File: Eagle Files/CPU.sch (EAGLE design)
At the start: 69 parts, among them IC1 74HC574N, IC10 74HC574N, IC11 74LS541N, IC12 CY62256LL-PC, IC13 74AS04N, IC14 74AS04N, IC15 74S283N, IC16 74S283N, IC19 74ALS04N, IC2 74LS541N, IC20 74LS541N, IC21 74LS08N, IC22 NE555, IC3 4514N, IC4 74LS04N, IC5 74HC574N, IC6 74LS541N, IC7 CY62256LL-PC, IC8 74S283N, IC9 74S283N

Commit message: Removed bugs
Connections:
- new net N$79: LED2.A, R2.2
- new net N$92: LED3.A, R3.2
- new net N$93: LED4.A, R4.2
- new net N$94: LED5.A, R5.2
- new net N$95: LED6.A, R6.2
- new net N$96: LED7.A, R7.2
- new net N$97: LED8.A, R8.2
- net BUS0: now also R1.1; no longer LED1.A, R1.2
- net BUS1: now also R2.1; no longer LED2.A, R2.2
- net BUS2: now also R3.1; no longer LED3.A, R3.2
- net BUS3: now also R4.1; no longer LED4.A, R4.2
- net BUS4: no longer LED5.A
- net BUS5: no longer LED6.A
- net BUS6: no longer LED7.A
- net BUS7: no longer LED8.A
- net GND: no longer R1.1, R2.1, R3.1, R4.1, R5.2, R6.2, R7.2, R8.2
- net N$17: now also IC13C.I
- net N$22: now also LED1.A, R1.2; no longer IC13C.I
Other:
- moved on the sheet: R1, R2, R3, R4, R5, R6, R7, R8

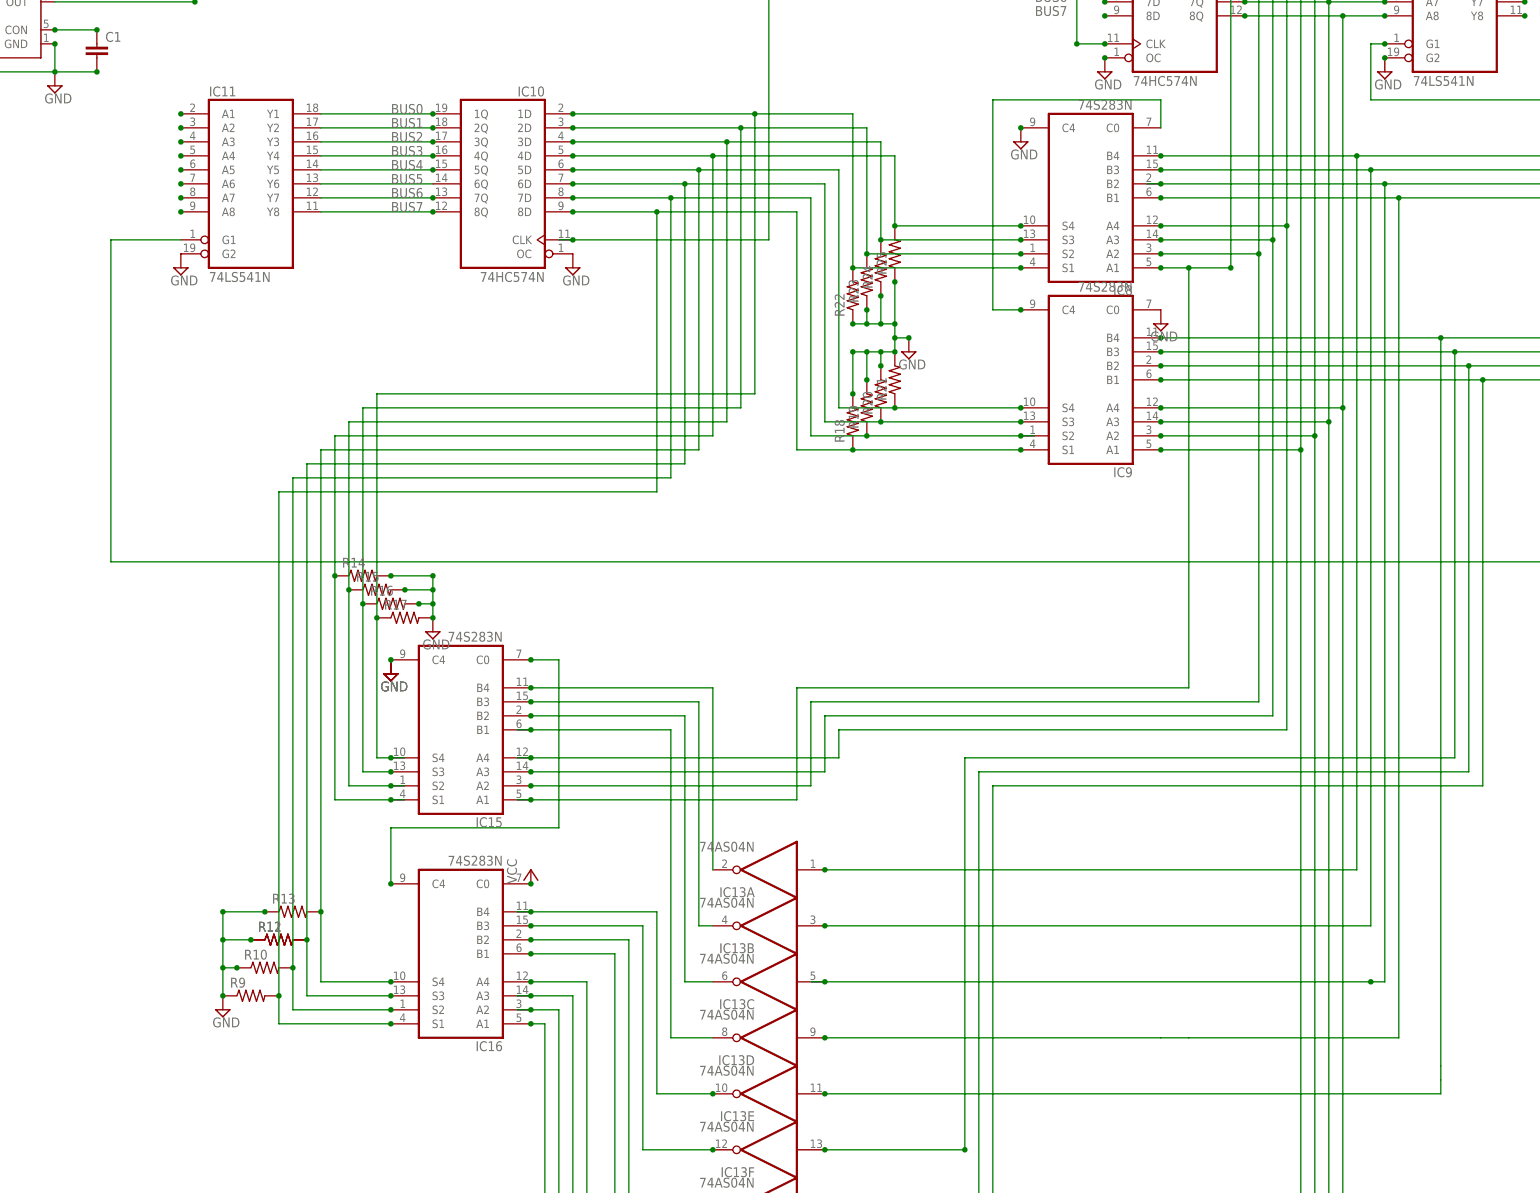
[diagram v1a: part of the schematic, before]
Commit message: Removed some bugs
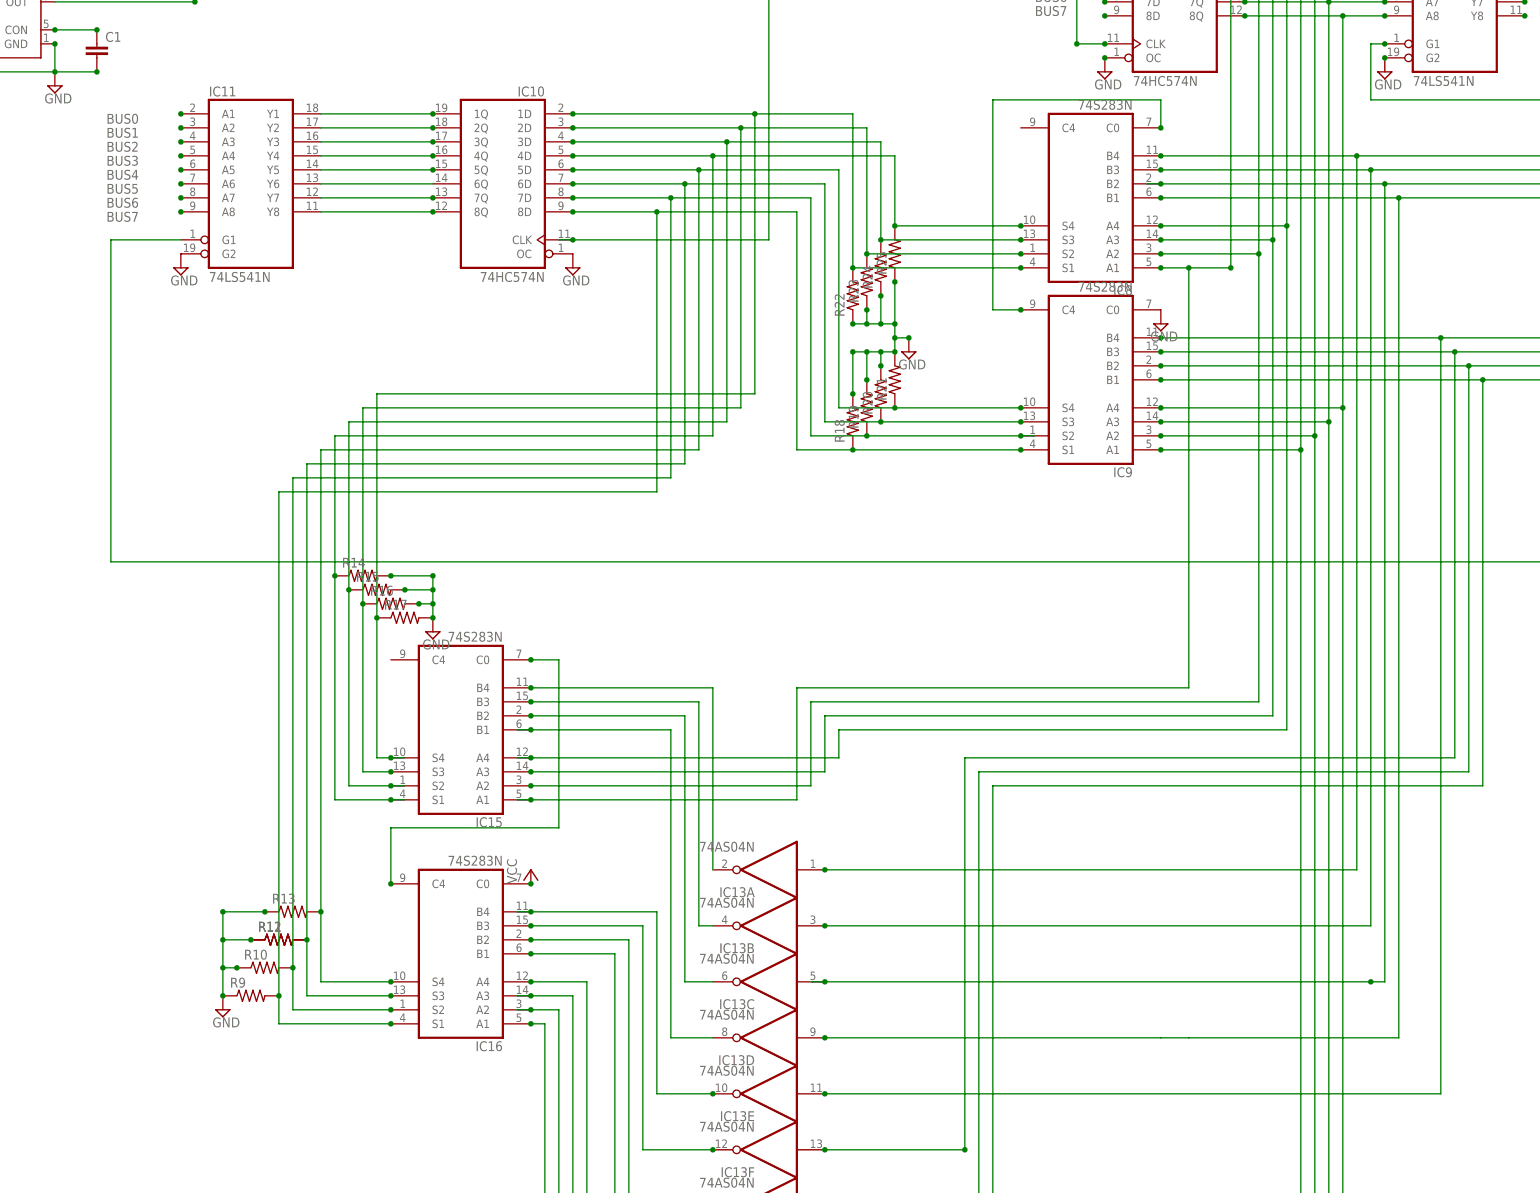
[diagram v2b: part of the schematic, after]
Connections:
- net GND: no longer IC15A.C4, IC8A.C4
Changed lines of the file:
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@@
 <part name="IC8" library="74xx-us" deviceset="74*283" device="N" technology="S"/>
 <part name="IC9" library="74xx-us" deviceset="74*283" device="N" technology="S"/>
-<part name="SUPPLY6" library="supply2" deviceset="GND" device=""/>
 <part name="IC10" library="74xx-us" deviceset="74*574" device="N" technology="HC"/>
 <part name="IC11" library="74xx-us" deviceset="74*541" device="N" technology="LS"/>
@@
 <part name="IC15" library="74xx-us" deviceset="74*283" device="N" technology="S"/>
 <part name="IC16" library="74xx-us" deviceset="74*283" device="N" technology="S"/>
-<part name="SUPPLY10" library="supply2" deviceset="GND" device=""/>
-<part name="SUPPLY11" library="supply2" deviceset="GND" device=""/>
 <part name="IC18" library="ic-package" deviceset="DIL16" device=""/>
 <part name="IC17" library="ic-package" deviceset="DIL16" device=""/>
@@
 <instance part="IC8" gate="A" x="66.04" y="27.94" rot="R180"/>
 <instance part="IC9" gate="A" x="66.04" y="-5.08" rot="R180"/>
-<instance part="SUPPLY6" gate="GND" x="53.34" y="38.1"/>
 <instance part="IC10" gate="A" x="-40.64" y="30.48" rot="MR0"/>
 <instance part="IC11" gate="A" x="-86.36" y="30.48"/>
@@
 <instance part="IC15" gate="A" x="-48.26" y="-68.58" rot="R180"/>
 <instance part="IC16" gate="A" x="-48.26" y="-109.22" rot="R180"/>
-<instance part="SUPPLY10" gate="GND" x="-60.96" y="-58.42"/>
-<instance part="SUPPLY11" gate="GND" x="-60.96" y="-58.42"/>
 <instance part="IC18" gate="G$1" x="-55.88" y="116.84" rot="R90"/>
 <instance part="IC17" gate="G$1" x="-91.44" y="116.84" rot="R90"/>
@@
 </segment>
 <segment>
-<pinref part="IC8" gate="A" pin="C4"/>
-<pinref part="SUPPLY6" gate="GND" pin="GND"/>
-<junction x="53.34" y="40.64"/>
-</segment>
-<segment>
 <pinref part="IC10" gate="A" pin="OC"/>
 <pinref part="SUPPLY8" gate="GND" pin="GND"/>
@@
 <pinref part="IC11" gate="A" pin="G2"/>
 <pinref part="SUPPLY9" gate="GND" pin="GND"/>
-</segment>
-<segment>
-<pinref part="IC15" gate="A" pin="C4"/>
-<pinref part="SUPPLY10" gate="GND" pin="GND"/>
-<pinref part="SUPPLY11" gate="GND" pin="GND"/>
-<junction x="-60.96" y="-55.88"/>
 </segment>
 <segment>
@@
 <wire x1="205.74" y1="2.54" x2="205.74" y2="66.04" width="0.1524" layer="91"/>
 <junction x="205.74" y="66.04"/>
-<wire x1="129.54" y1="-132.08" x2="129.54" y2="-129.54" width="0.1524" layer="91"/>
 <pinref part="IC13" gate="E" pin="I"/>
 <junction x="17.78" y="-134.62"/>
-<wire x1="129.54" y1="-129.54" x2="129.54" y2="2.54" width="0.1524" layer="91"/>
+<wire x1="129.54" y1="-134.62" x2="129.54" y2="2.54" width="0.1524" layer="91"/>
 <wire x1="129.54" y1="-134.62" x2="17.78" y2="-134.62" width="0.1524" layer="91"/>
-<wire x1="129.54" y1="-132.08" x2="129.54" y2="-134.62" width="0.1524" layer="91"/>
 <junction x="129.54" y="2.54"/>
 <junction x="78.74" y="2.54"/>
@@
 <pinref part="IC11" gate="A" pin="A2"/>
 <junction x="-99.06" y="40.64"/>
-<label x="-60.96" y="40.64" size="1.778" layer="95"/>
+<label x="-106.68" y="40.64" size="1.778" layer="95" rot="R180"/>
 </segment>
 <segment>
@@
 <pinref part="IC11" gate="A" pin="A3"/>
 <junction x="-99.06" y="38.1"/>
-<label x="-60.96" y="38.1" size="1.778" layer="95"/>
+<label x="-106.68" y="38.1" size="1.778" layer="95" rot="R180"/>
 </segment>
 <segment>
@@
 <pinref part="IC11" gate="A" pin="A4"/>
 <junction x="-99.06" y="35.56"/>
-<label x="-60.96" y="35.56" size="1.778" layer="95"/>
+<label x="-106.68" y="35.56" size="1.778" layer="95" rot="R180"/>
 </segment>
 <segment>
@@
 <pinref part="IC11" gate="A" pin="A5"/>
 <junction x="-99.06" y="33.02"/>
-<label x="-60.96" y="33.02" size="1.778" layer="95"/>
+<label x="-106.68" y="33.02" size="1.778" layer="95" rot="R180"/>
 </segment>
 <segment>
@@
 <pinref part="IC11" gate="A" pin="A6"/>
 <junction x="-99.06" y="30.48"/>
-<label x="-60.96" y="30.48" size="1.778" layer="95"/>
+<label x="-106.68" y="30.48" size="1.778" layer="95" rot="R180"/>
 </segment>
 <segment>
@@
 <pinref part="IC11" gate="A" pin="A7"/>
 <junction x="-99.06" y="27.94"/>
-<label x="-60.96" y="27.94" size="1.778" layer="95"/>
+<label x="-106.68" y="27.94" size="1.778" layer="95" rot="R180"/>
 </segment>
 <segment>
@@
 <pinref part="IC11" gate="A" pin="A8"/>
 <junction x="-99.06" y="25.4"/>
-<label x="-60.96" y="25.4" size="1.778" layer="95"/>
+<label x="-106.68" y="25.4" size="1.778" layer="95" rot="R180"/>
 </segment>
 <segment>
@@
 <pinref part="IC11" gate="A" pin="A1"/>
 <junction x="-99.06" y="43.18"/>
-<label x="-60.96" y="43.18" size="1.778" layer="95"/>
+<label x="-106.68" y="43.18" size="1.778" layer="95" rot="R180"/>
 </segment>
 <segment>
@@
 <wire x1="30.48" y1="-10.16" x2="20.32" y2="-10.16" width="0.1524" layer="91"/>
 <wire x1="20.32" y1="-10.16" x2="20.32" y2="33.02" width="0.1524" layer="91"/>
-<wire x1="20.32" y1="33.02" x2="0" y2="33.02" width="0.1524" layer="91"/>
+<wire x1="20.32" y1="33.02" x2="-5.08" y2="33.02" width="0.1524" layer="91"/>
 <pinref part="IC10" gate="A" pin="5D"/>
 <junction x="-27.94" y="33.02"/>
 <wire x1="-27.94" y1="33.02" x2="-5.08" y2="33.02" width="0.1524" layer="91"/>
 <pinref part="IC16" gate="A" pin="S4"/>
-<wire x1="-5.08" y1="33.02" x2="0" y2="33.02" width="0.1524" layer="91"/>
 <wire x1="-60.96" y1="-114.3" x2="-73.66" y2="-114.3" width="0.1524" layer="91"/>
 <wire x1="-73.66" y1="-114.3" x2="-73.66" y2="-101.6" width="0.1524" layer="91"/>
@@
 <wire x1="25.4" y1="-15.24" x2="15.24" y2="-15.24" width="0.1524" layer="91"/>
 <wire x1="15.24" y1="-15.24" x2="15.24" y2="27.94" width="0.1524" layer="91"/>
-<wire x1="15.24" y1="27.94" x2="0" y2="27.94" width="0.1524" layer="91"/>
+<wire x1="15.24" y1="27.94" x2="-10.16" y2="27.94" width="0.1524" layer="91"/>
 <pinref part="IC10" gate="A" pin="7D"/>
 <junction x="-27.94" y="27.94"/>
 <wire x1="-27.94" y1="27.94" x2="-10.16" y2="27.94" width="0.1524" layer="91"/>
 <pinref part="IC16" gate="A" pin="S2"/>
-<wire x1="-10.16" y1="27.94" x2="0" y2="27.94" width="0.1524" layer="91"/>
 <wire x1="-60.96" y1="-119.38" x2="-78.74" y2="-119.38" width="0.1524" layer="91"/>
 <wire x1="-78.74" y1="-119.38" x2="-78.74" y2="-111.76" width="0.1524" layer="91"/>
@@
 <wire x1="78.74" y1="45.72" x2="78.74" y2="40.64" width="0.1524" layer="91"/>
 <junction x="53.34" y="7.62"/>
-</segment>
-</net>
+<junction x="78.74" y="40.64"/>
+</segment>
+</net>

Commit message: Removed some bugs
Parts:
- removed IC17, IC18: (no value), ic-package:DIL16
- removed IC19: 74ALS04N, 74xx-us:74ALS04N
- removed IC20: 74LS541N, 74xx-us:74LS541N
- removed IC21: 74LS08N, 74xx-us:74LS08N
- removed IC22: NE555, st-microelectronics:NE555
- removed R31, R32, R33, R34, R35, R36, R37: (no value), resistor:R-US_0204/2V
- added D1, D10, D11, D12, D13, D14, D15, D16, D2, D3, D4, D5, D6, D7, D8, D9: 1N4148DO35-7, diode:1N4148DO35-7
- C1, C2: device rcl:C-EU025-024X044 -> capacitor-wima:C2,5-3
- IC1: value 74HC574N -> 74AS574N; device 74xx-us:74HC574N -> 74xx-us:74AS574N
- IC10: value 74HC574N -> 74AC283N; device 74xx-us:74HC574N -> 74xx-eu:74AC283N
- IC11, IC2: value 74LS541N -> 74AS574N; device 74xx-us:74LS541N -> 74xx-us:74AS574N
- IC12: value CY62256LL-PC -> 74LS541N; device memory-sram:CY62256LL-PC -> 74xx-us:74LS541N
- IC13: value 74AS04N -> 74HC393N; device 74xx-us:74AS04N -> 74xx-eu:74HC393N
- IC14: value 74AS04N -> 74LS541N; device 74xx-us:74AS04N -> 74xx-us:74LS541N
- IC15: value 74S283N -> 74LS32N; device 74xx-us:74S283N -> 74xx-us:74LS32N
- IC16: value 74S283N -> NE555; device 74xx-us:74S283N -> st-microelectronics:NE555
- IC3: value 4514N -> 74LS541N; device 45xx:4514N -> 74xx-us:74LS541N
- IC4: value 74LS04N -> 74LS541N; device 74xx-us:74LS04N -> 74xx-us:74LS541N
- IC5: value 74HC574N -> CY62256LL-PC; device 74xx-us:74HC574N -> memory-sram:CY62256LL-PC
- IC6: value 74LS541N -> CY62256LL-PC; device 74xx-us:74LS541N -> memory-sram:CY62256LL-PC
- IC7: value CY62256LL-PC -> 4514N; device memory-sram:CY62256LL-PC -> 45xx:4514N
- IC8: value 74S283N -> 74HC04N; device 74xx-us:74S283N -> 74xx-eu:74HC04N
- IC9: value 74S283N -> 74AC283N; device 74xx-us:74S283N -> 74xx-eu:74AC283N
- LED1, LED2, LED3, LED4, LED5, LED6, LED7, LED8: device eagle-ltspice:LED_ELD260 -> led:LED3MM
- R1, R10, R11, R12, R13, R14, R15, R16, R17, R2, R26, R27, R28, R29, R3, R30, R4, R5, R6, R7, R8, R9: device resistor:R-US_0204/2V -> rcl:R-US_MELF0102AX
- R18, R19, R20, R21, R22, R23, R24, R25: device rcl:R-US_0204/2V -> rcl:R-US_MELF0102AX
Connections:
- removed net BUS0: IC11A.A1, IC17.P0, IC1A.1D, IC20A.Y1, IC2A.Y1, IC5A.1D, IC6A.Y1, R1.1
- removed net BUS1: IC11A.A2, IC17.P1, IC1A.2D, IC20A.Y2, IC2A.Y2, IC3A.S2, IC5A.2D, IC5A.CLK, IC6A.Y2, R2.1
- removed net BUS2: IC11A.A3, IC17.P2, IC1A.3D, IC20A.Y3, IC2A.Y3, IC5A.3D, IC6A.Y3, R3.1
- removed net BUS3: IC11A.A4, IC17.P3, IC1A.4D, IC1A.CLK, IC20A.Y4, IC2A.Y4, IC3A.S0, IC5A.4D, IC6A.Y4, R4.1
- removed net BUS4: IC11A.A5, IC18.P0, IC1A.5D, IC20A.Y5, IC2A.Y5, IC5A.5D, IC6A.Y5, R5.1
- removed net BUS5: IC11A.A6, IC18.P1, IC1A.6D, IC20A.Y6, IC2A.Y6, IC5A.6D, IC6A.Y6, R6.1
- removed net BUS6: IC11A.A7, IC18.P2, IC1A.7D, IC20A.Y7, IC2A.Y7, IC5A.7D, IC6A.Y7, R7.1
- removed net BUS7: IC11A.A8, IC18.P3, IC1A.8D, IC20A.Y8, IC2A.Y8, IC5A.8D, IC6A.Y8, R8.1
- new net N$100: LED5.A, R24.2
- new net N$101: LED6.A, R25.2
- new net N$102: LED7.A, R26.2
- new net N$103: LED8.A, R27.2
- new net N$104: IC7A.S5, IC8C.I
- new net N$105: IC12A.G1, IC8C.O
- new net N$106: D16.C, IC2A.8D
- new net N$107: D11.A, D3.A, IC14A.Y3
- new net N$108: D1.A, D9.A, IC14A.Y1
- new net N$109: D12.A, D4.A, IC14A.Y4
- new net N$110: D14.A, D6.A, IC14A.Y6
- new net N$111: D15.A, D7.A, IC14A.Y7
- new net N$112: D16.A, D8.A, IC14A.Y8
- new net N$113: D13.A, D5.A, IC14A.Y5
- new net N$114: D10.A, D2.A, IC14A.Y2
- new net N$115: IC15A.O, IC8D.I
- new net N$116: D1.C, IC1A.1D
- new net N$117: D2.C, IC1A.2D
- new net N$118: D3.C, IC1A.3D
- new net N$119: D4.C, IC1A.4D
- new net N$120: D5.C, IC1A.5D
- new net N$121: D6.C, IC1A.6D
- new net N$122: D7.C, IC1A.7D
- new net N$123: D8.C, IC1A.8D
- new net N$124: IC14A.G2, IC8D.O
- new net N$125: R29.1, R30.2
- new net N$126: IC16.DIS, R28.1, R29.2
- new net N$127: C1.1, IC16.TRE, IC16.TRI, R30.1
- new net N$128: IC13A.A, IC13B.A, IC8E.O
- new net N$130: IC16.OUT, IC8E.I
- new net N$98: LED3.A, R21.2
- new net N$99: LED4.A, R23.2
- net GND: now also IC10A.C0, IC11A.OC, IC12A.G2, IC13A.CLR, IC13B.CLR, IC14A.G1, IC16.GND, IC2A.OC, IC3A.G2, IC4A.G2, IC5G$1.!CE, IC5G$1.!OE, IC6G$1.!CE, IC6G$1.!OE, IC7A.ST, R1.1, R14.1, R15.1, R16.1, R17.1, R18.1, R2.1, R3.1, R4.1, R5.1, R6.1, R7.1, R8.1; no longer IC10A.OC, IC11A.G2, IC12G$1.!CE, IC12G$1.!OE, IC12G$1.A10, IC12G$1.A11, IC12G$1.A12, IC12G$1.A13, IC12G$1.A14, IC12G$1.A8, IC12G$1.A9, IC17.GND, IC18.GND, IC20A.G2, IC22.GND, IC2A.G2, IC3A.INH, IC5A.OC, IC6A.G2, IC7G$1.!CE, IC7G$1.!OE, IC7G$1.A10, IC7G$1.A11, IC7G$1.A12, IC7G$1.A13, IC7G$1.A14, IC7G$1.A8, IC7G$1.A9, IC9A.C0, R14.2, R15.2, R16.2, R17.2, R18.2, R20.2, R21.2, R22.1, R23.1, R24.1, R25.1, R26.2, R27.2, R28.2, R29.2, R30.2, R31.2, R32.2, R33.2, R34.2
- net N$1: now also IC3A.A1, IC9A.A1; no longer IC15A.A1, IC2A.A1, IC8A.A1
- net N$10: now also IC2A.3Q, IC4A.A3, IC9A.B3; no longer IC3A.D2, IC7G$1.DQ1
- net N$11: now also IC2A.4Q, IC4A.A4, IC9A.B4; no longer IC3A.D3, IC7G$1.DQ2
- net N$12: now also IC10A.B1, IC2A.5Q, IC4A.A5; no longer IC3A.D4, IC7G$1.DQ3
- net N$13: now also IC10A.B2, IC2A.6Q, IC4A.A6; no longer IC3A.S1, IC4A.I
- net N$14: now also IC10A.B3, IC2A.7Q, IC4A.A7; no longer IC21A.I0, IC2A.G1, IC4A.O
- net N$15: now also IC10A.B4, IC2A.8Q, IC4A.A8; no longer IC13A.O, IC15A.B4
- net N$16: now also IC10A.A4, IC1A.8Q, IC3A.A8; no longer IC13B.O, IC15A.B3
- net N$17: now also IC13B.QB, IC5G$1.A5, IC6G$1.A5; no longer IC13C.I, IC5A.3Q, IC6A.A3, IC8A.B2
- net N$18: now also C2.1, IC16.CON; no longer IC13D.I, IC5A.4Q, IC6A.A4, IC8A.B1
- net N$19: now also IC13A.QB, IC5G$1.A1, IC6G$1.A1; no longer IC13E.I, IC5A.5Q, IC6A.A5, IC9A.B4
- net N$2: now also IC3A.A2, IC9A.A2; no longer IC15A.A2, IC2A.A2, IC8A.A2
- net N$20: now also IC13A.QC, IC5G$1.A2, IC6G$1.A2; no longer IC13F.I, IC5A.6Q, IC6A.A6, IC9A.B3
- net N$21: now also IC13A.QD, IC5G$1.A3, IC6G$1.A3; no longer IC14A.I, IC5A.7Q, IC6A.A7, IC9A.B2
- net N$22: now also IC13B.QA, IC5G$1.A4, IC6G$1.A4; no longer LED1.A, R1.2
- net N$23: now also IC13B.QC, IC5G$1.A6, IC6G$1.A6; no longer IC21A.I1, IC4B.O, IC6A.G1
- net N$24: now also IC13B.QD, IC5G$1.A7, IC6G$1.A7; no longer IC3A.S3, IC4B.I
- net N$25: now also IC14A.A1, IC5G$1.DQ0; no longer IC15A.A4, IC1A.4Q, IC2A.A4, IC8A.A4
- net N$26: now also IC14A.A2, IC5G$1.DQ1; no longer IC8A.C0, IC9A.C4
- net N$27: now also IC14A.A3, IC5G$1.DQ2; no longer IC10A.1D, IC15A.S4, IC8A.S1, R17.1, R22.2
- net N$28: now also IC14A.A4, IC5G$1.DQ3; no longer IC10A.2D, IC15A.S3, IC8A.S2, R16.1, R23.2
- net N$29: now also IC14A.A5, IC5G$1.DQ4; no longer IC10A.3D, IC15A.S2, IC8A.S3, R15.1, R24.2
- net N$3: now also IC3A.A3, IC9A.A3; no longer IC15A.A3, IC2A.A3, IC8A.A3
- net N$30: now also IC14A.A6, IC5G$1.DQ5; no longer IC10A.4D, IC15A.S1, IC8A.S4, R14.1, R25.2
- net N$31: now also IC14A.A7, IC5G$1.DQ6; no longer IC10A.5D, IC16A.S4, IC9A.S4, R13.2, R21.1
- net N$32: now also IC14A.A8, IC5G$1.DQ7; no longer IC10A.6D, IC16A.S3, IC9A.S3, R11.2, R12.2, R20.1
- net N$33: now also IC5G$1.A8, R1.2; no longer IC10A.7D, IC16A.S2, IC9A.S2, R10.2, R19.1
- net N$34: now also IC5G$1.A9, R2.2; no longer IC10A.8D, IC16A.S1, IC9A.S1, R18.1, R9.2
- net N$35: now also IC5G$1.A10, R3.2; no longer IC10A.1Q, IC11A.Y1
- net N$36: now also IC5G$1.A11, R4.2; no longer IC10A.2Q, IC11A.Y2
- net N$37: now also IC5G$1.A12, R5.2; no longer IC10A.3Q, IC11A.Y3
- net N$38: now also IC5G$1.A13, R6.2; no longer IC10A.4Q, IC11A.Y4
- net N$39: now also IC5G$1.A14, R7.2; no longer IC10A.5Q, IC11A.Y5
- net N$4: now also IC1A.4Q, IC3A.A4, IC9A.A4; no longer IC16A.A3, IC1A.6Q, IC2A.A6, IC9A.A2
- net N$40: now also IC6G$1.DQ0, IC7A.D1; no longer IC10A.6Q, IC11A.Y6
- net N$41: now also IC6G$1.A8, R8.2; no longer IC10A.7Q, IC11A.Y7
- net N$42: now also IC6G$1.A9, R9.2; no longer IC10A.8Q, IC11A.Y8
- net N$43: now also IC6G$1.A10, R10.2; no longer IC10A.CLK, IC3A.S4
- net N$44: now also IC6G$1.A11, R11.2; no longer IC3A.S5, IC4C.I
- net N$45: now also IC6G$1.A12, R12.2; no longer IC11A.G1, IC21B.I1, IC4C.O
- net N$46: now also IC6G$1.A13, R13.2; no longer IC12G$1.A0, IC17.Q0, IC7G$1.A0
- net N$47: now also IC6G$1.A14, R14.2; no longer IC12G$1.A1, IC17.Q1, IC7G$1.A1
- net N$48: now also IC6G$1.DQ1, IC7A.D2; no longer IC12G$1.A2, IC17.Q2, IC7G$1.A2
- net N$49: now also IC6G$1.DQ2, IC7A.D3; no longer IC12G$1.A3, IC17.Q3, IC7G$1.A3
- net N$5: now also IC10A.A1, IC3A.A5; no longer IC16A.A4, IC2A.A5, IC9A.A1
- net N$50: now also IC6G$1.DQ3, IC7A.D4; no longer IC12G$1.A4, IC18.Q0, IC7G$1.A4
- net N$51: now also IC6G$1.DQ4, R15.2; no longer IC12G$1.A5, IC18.Q1, IC7G$1.A5
- net N$52: now also IC6G$1.DQ5, R16.2; no longer IC12G$1.A6, IC18.Q2, IC7G$1.A6
- net N$53: now also IC6G$1.DQ6, R17.2; no longer IC12G$1.A7, IC18.Q3, IC7G$1.A7
- net N$54: now also IC6G$1.DQ7, R18.2; no longer IC12G$1.DQ0, IC20A.A1
- net N$55: now also D9.C, IC2A.1D; no longer IC12G$1.DQ1, IC20A.A2
- net N$56: now also D10.C, IC2A.2D; no longer IC12G$1.DQ2, IC20A.A3
- net N$57: now also D11.C, IC2A.3D; no longer IC12G$1.DQ3, IC20A.A4
- net N$58: now also D12.C, IC2A.4D; no longer IC12G$1.DQ4, IC20A.A5
- net N$59: now also D13.C, IC2A.5D; no longer IC12G$1.DQ5, IC20A.A6
- net N$6: now also IC10A.A2, IC1A.6Q, IC3A.A6; no longer IC20A.G1, IC4D.O
- net N$60: now also D14.C, IC2A.6D; no longer IC12G$1.DQ6, IC20A.A7
- net N$61: now also D15.C, IC2A.7D; no longer IC13B.I, IC5A.2Q, IC6A.A2, IC8A.B3
- net N$62: now also IC13A.QA, IC5G$1.A0, IC6G$1.A0; no longer IC13A.I, IC5A.1Q, IC6A.A1, IC8A.B4
- net N$63: now also IC11A.CLK, IC7A.S4; no longer IC13C.O, IC15A.B2
- net N$64: now also IC15A.I0, IC2A.CLK, IC7A.S2; no longer IC13D.O, IC15A.B1
- net N$65: now also IC15A.I1, IC1A.CLK, IC7A.S0; no longer IC13E.O, IC16A.B4
- net N$66: now also IC7A.S1, IC8B.I; no longer IC13F.O, IC16A.B3
- net N$67: now also IC3A.G1, IC8B.O; no longer IC14B.I, IC5A.8Q, IC6A.A8, IC9A.B1
- net N$68: now also IC4A.G1, IC8A.O; no longer IC14A.O, IC16A.B2
- net N$69: now also IC7A.S3, IC8A.I; no longer IC14B.O, IC16A.B1
- net N$7: now also IC10A.A3, IC3A.A7; no longer IC16A.A2, IC2A.A7, IC9A.A3
- net N$70: now also IC10A.C4, IC9A.C0; no longer IC17.CP, IC22.OUT
- net N$71: now also IC9A.C4, R19.1; no longer IC17.TC, IC18.CP
- net N$72: now also IC11A.1D, IC9A.S1; no longer IC19A.I, IC3A.S6
- net N$73: now also IC11A.2D, IC9A.S2; no longer IC17.|SPE, IC18.|SPE, IC19A.O
- net N$74: now also IC11A.3D, IC9A.S3; no longer IC15A.C0, IC16A.C4
- net N$75: now also IC11A.4D, IC9A.S4; no longer IC21B.O, IC4D.I
- net N$76: now also IC10A.S1, IC11A.5D; no longer IC21B.I0
- net N$77: now also IC10A.S2, IC11A.6D; no longer IC12G$1.DQ7, IC20A.A8
- net N$78: now also IC10A.S3, IC11A.7D; no longer IC3A.S7, R26.1
- net N$79: now also IC10A.S4, IC11A.8D; no longer LED2.A, R2.2
- net N$8: now also IC2A.1Q, IC4A.A1, IC9A.B1; no longer IC16A.A1, IC1A.8Q, IC2A.A8, IC9A.A4
- net N$80: now also IC11A.1Q, IC12A.A1; no longer IC3A.S8, R27.1
- net N$81: now also IC11A.2Q, IC12A.A2; no longer IC3A.S9, R28.1
- net N$82: now also IC11A.3Q, IC12A.A3; no longer IC3A.S10, R29.1
- net N$83: now also IC11A.4Q, IC12A.A4; no longer IC3A.S11, R30.1
- net N$84: now also IC11A.5Q, IC12A.A5; no longer IC3A.S12, R31.1
- net N$85: now also IC11A.6Q, IC12A.A6; no longer IC3A.S13, R32.1
- net N$86: now also IC11A.7Q, IC12A.A7; no longer IC3A.S14, R33.1
- net N$87: now also IC11A.8Q, IC12A.A8; no longer IC3A.S15, R34.1
- net N$88: now also IC12A.Y1, R20.1; no longer C1.1, IC22.CON
- net N$89: now also IC12A.Y3, R21.1; no longer IC22.DIS, R35.1, R37.2
- net N$9: now also IC2A.2Q, IC4A.A2, IC9A.B2; no longer IC3A.D1, IC7G$1.DQ0
- net N$90: now also IC12A.Y2, R22.1; no longer C2.1, IC22.TRE, IC22.TRI, R36.1
- net N$91: now also IC12A.Y4, R23.1; no longer R36.2, R37.1
- net N$92: now also IC12A.Y5, R24.1; no longer LED3.A, R3.2
- net N$93: now also IC12A.Y6, R25.1; no longer LED4.A, R4.2
- net N$94: now also IC12A.Y7, R26.1; no longer LED5.A, R5.2
- net N$95: now also IC12A.Y8, R27.1; no longer LED6.A, R6.2
- net N$96: now also LED1.A, R20.2; no longer LED7.A, R7.2
- net N$97: now also LED2.A, R22.2; no longer LED8.A, R8.2
- net VCC: now also IC16./RES, IC16.VCC+, IC5G$1.!WE, IC6G$1.!WE, IC7A.INH, R28.2; no longer IC12G$1.!WE, IC16A.C0, IC17.PE, IC17.TE, IC17.VCC, IC17.|MR, IC18.PE, IC18.TE, IC18.VCC, IC18.|MR, IC22./RES, IC22.VCC+, IC3A.ST, IC7G$1.!WE, R35.2
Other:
- note added: "ADD"
- note added: "LODA"
- note added: "LODB"
- note added: "OUTPUT"
- note added: "READA"
- note added: "READB"
- note added: "REGISTER A"
- note added: "REGISTER B"
- note removed: "Clock"
- note removed: "Load A"
- note removed: "Load B"
- note removed: "Load C"
- note removed: "Read A"
- note removed: "Read B"
- note removed: "Read C"
- note removed: "jump"
- moved on the sheet: C1, C2, IC1, IC11, IC2, IC9, LED1, LED2, LED3, LED4, LED5, LED6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

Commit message: Removed bugs
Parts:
- added IC18: 74LS541N, 74xx-us:74LS541N
- added LED10, LED11, LED12, LED13, LED14, LED15, LED16, LED17, LED18, LED19, LED20, LED21, LED22, LED23, LED24, LED9: (no value), led:LED3MM
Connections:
- new net N$129: IC15B.I0, IC18A.G2, IC8F.O
- new net N$131: IC15B.O, IC1A.CLK
- new net N$132: IC7A.S6, IC8F.I
- new net N$133: IC3A.Y1, LED9.A
- new net N$134: IC3A.Y2, LED10.A
- new net N$135: IC3A.Y3, LED11.A
- new net N$136: IC3A.Y4, LED12.A
- new net N$137: IC3A.Y5, LED13.A
- new net N$138: IC3A.Y6, LED14.A
- new net N$139: IC3A.Y7, LED15.A
- new net N$140: IC3A.Y8, LED16.A
- new net N$141: IC4A.Y1, LED17.A
- new net N$142: IC4A.Y2, LED18.A
- new net N$143: IC4A.Y3, LED19.A
- new net N$144: IC4A.Y4, LED20.A
- new net N$145: IC4A.Y5, LED21.A
- new net N$146: IC4A.Y6, LED22.A
- new net N$147: IC4A.Y7, LED23.A
- new net N$148: IC4A.Y8, LED24.A
- net GND: now also IC18A.G1, LED10.C, LED11.C, LED12.C, LED13.C, LED14.C, LED15.C, LED16.C, LED17.C, LED18.C, LED19.C, LED20.C, LED21.C, LED22.C, LED23.C, LED24.C, LED9.C
- net N$100: now also IC18A.A3, LED6.A, R25.2; no longer LED5.A, R24.2
- net N$101: now also IC18A.A5, LED4.A, R23.2; no longer LED6.A, R25.2
- net N$102: now also IC18A.A6, LED3.A, R21.2; no longer LED7.A, R26.2
- net N$103: now also IC18A.A8, LED1.A, R20.2; no longer LED8.A, R27.2
- net N$107: now also IC18A.Y3
- net N$108: now also IC18A.Y1
- net N$109: now also IC18A.Y4
- net N$110: now also IC18A.Y6
- net N$111: now also IC18A.Y7
- net N$112: now also IC18A.A7, LED2.A, R22.2; no longer D16.A, D8.A, IC14A.Y8
- net N$113: now also IC18A.Y5
- net N$114: now also IC18A.Y2
- net N$65: now also IC15B.I1; no longer IC1A.CLK
- net N$96: now also D16.A, D8.A, IC14A.Y8, IC18A.Y8; no longer LED1.A, R20.2
- net N$97: now also IC18A.A4, LED5.A, R24.2; no longer LED2.A, R22.2
- net N$98: now also IC18A.A2, LED7.A, R26.2; no longer LED3.A, R21.2
- net N$99: now also IC18A.A1, LED8.A, R27.2; no longer LED4.A, R23.2
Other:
- note added: "RETURN"
- moved on the sheet: LED1, LED2, LED3, LED4, LED5, LED6, LED7, LED8
